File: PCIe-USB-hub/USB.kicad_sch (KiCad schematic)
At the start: 8 parts, among them J2 USB3_A_Stacked, J3 USB3_A_Stacked, J4 USB3_A_Stacked, J5 USB3_A_Stacked, J6 USB3_A_Stacked, J7 USB3_A_Stacked, J8 USB3_A_Stacked, J9 USB3_A_Stacked

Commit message: Частично добавил компоненты
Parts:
- removed J7, J8, J9: USB3_A_Stacked, Connector_USB:USB3_A_Molex_48406-0001_Horizontal_Stacked, symbol Connector:USB3_A_Stacked
- added C1, C10, C2, C3, C4, C5, C6, C7, C8, C9: EEEFK1E151P, Capacitor_SMD:C_Elec_8x10.2, symbol Device:C_Polarized
- added DD3: TPS2552DRVR, Package_SON:WSON-6-1EP_2x2mm_P0.65mm_EP1x1.6mm, symbol TPS2552DRVR:TPS2552DRVR
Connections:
- net at J4.10 (VBUS2): now also C3.1
- net at J3.10 (VBUS2): now also C9.1
- net at J6.10 (VBUS2): now also C6.1
- net at J5.1 (VBUS1): now also C7.1
- net at J5.10 (VBUS2): now also C10.1
- net at J6.1 (VBUS1): now also C5.1
- net at J2.10 (VBUS2): now also C2.1
- net at J3.1 (VBUS1): now also C8.1
- net at J4.1 (VBUS1): now also C4.1
- net at J2.1 (VBUS1): now also C1.1
- new net Earth: C1.2, C10.2, C2.2, C3.2, C4.2, C5.2, C6.2, C7.2, C8.2, C9.2
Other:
- moved on the sheet: J2A, J2B, J3A, J3B, J4A, J4B, J5A, J5B, J6A, J6B

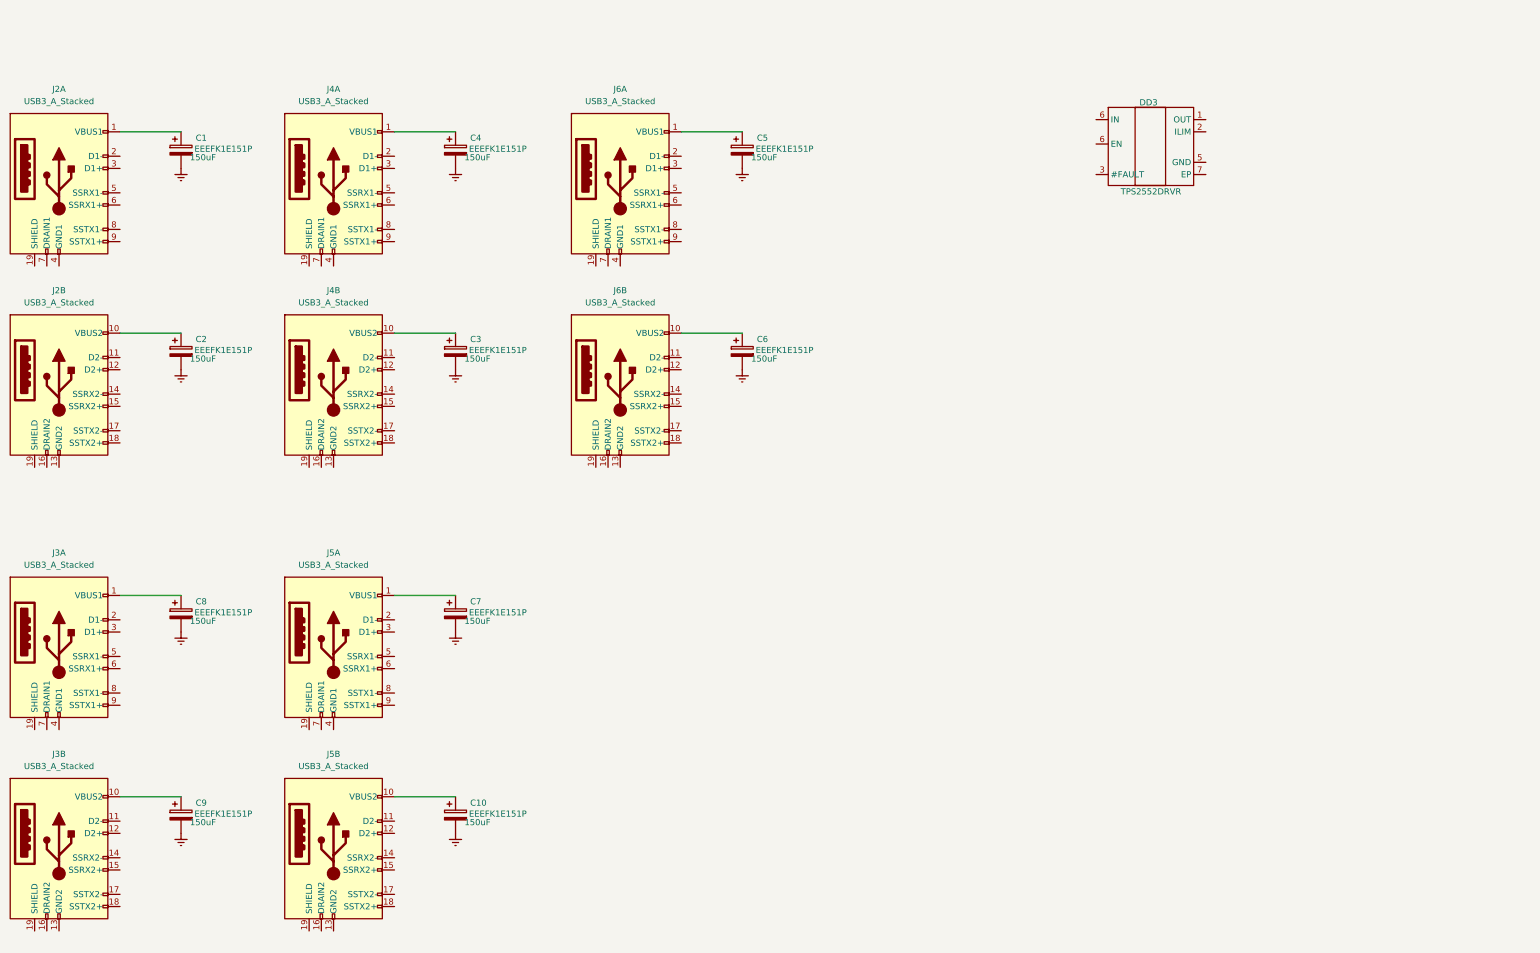
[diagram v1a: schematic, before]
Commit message: Изменение иерархии схемы + на схеме теперь все линии USB соединены
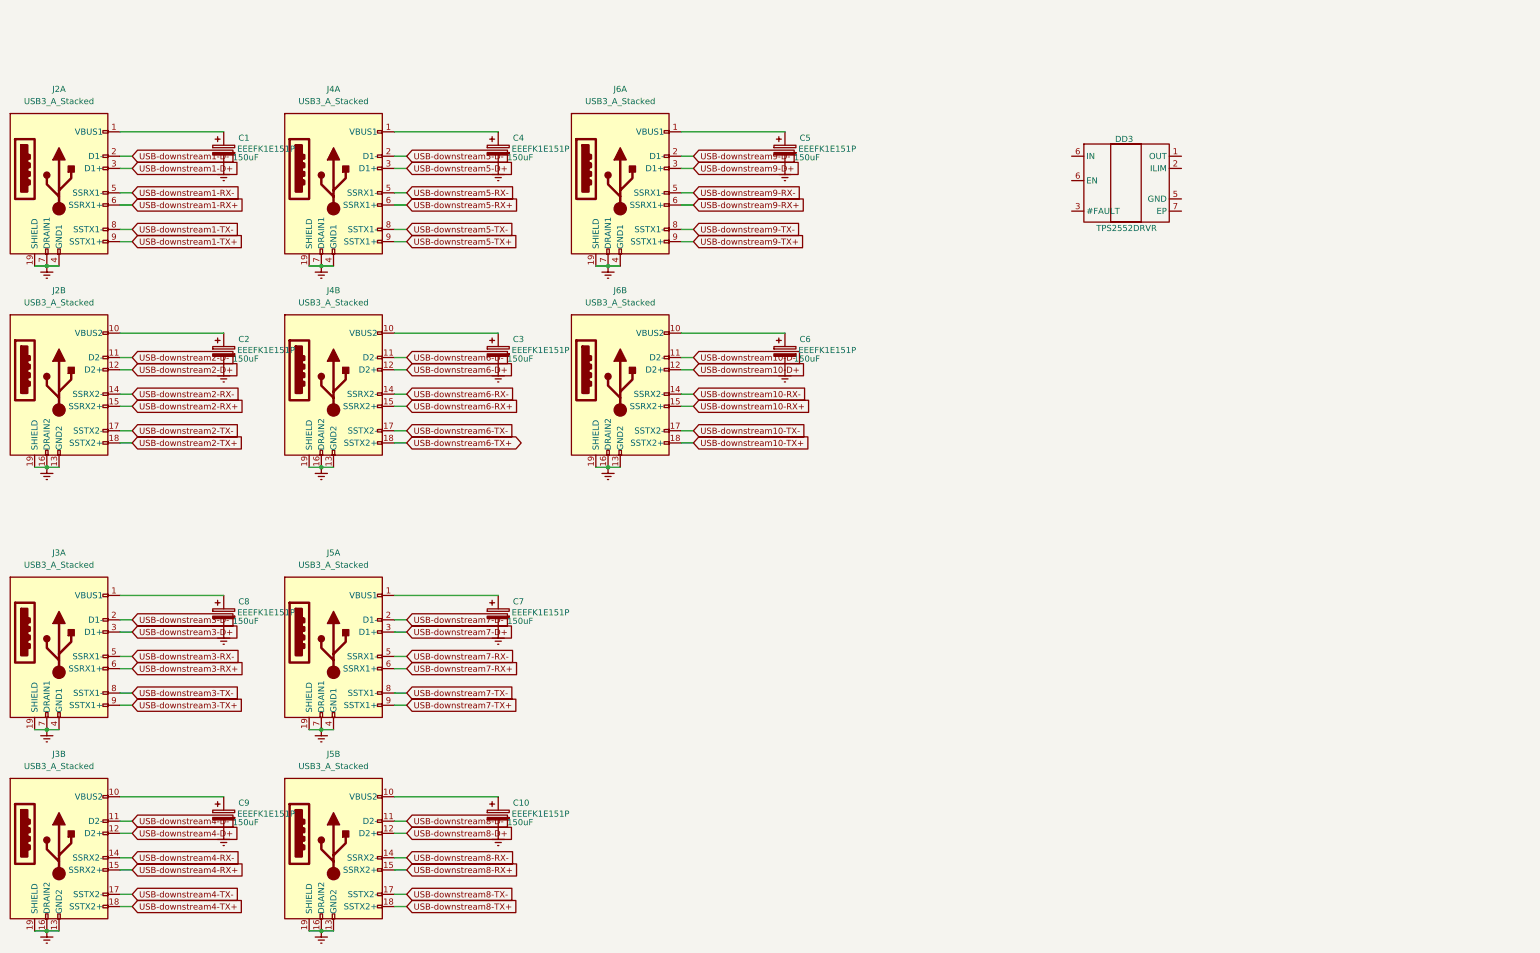
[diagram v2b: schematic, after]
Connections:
- net Earth: now also J2.13 (GND2), J2.16 (DRAIN2), J2.19 (SHIELD), J2.19 (SHIELD), J2.4 (GND1), J2.7 (DRAIN1), J3.13 (GND2), J3.16 (DRAIN2), J3.19 (SHIELD), J3.19 (SHIELD), J3.4 (GND1), J3.7 (DRAIN1), J4.13 (GND2), J4.16 (DRAIN2), J4.19 (SHIELD), J4.19 (SHIELD), J4.4 (GND1), J4.7 (DRAIN1), J5.13 (GND2), J5.16 (DRAIN2), J5.19 (SHIELD), J5.19 (SHIELD), J5.4 (GND1), J5.7 (DRAIN1), J6.13 (GND2), J6.16 (DRAIN2), J6.19 (SHIELD), J6.19 (SHIELD), J6.4 (GND1), J6.7 (DRAIN1)
- net USB-downstream6-D-: now reaches J4.11 (D2-)
- net USB-downstream6-D+: now reaches J4.12 (D2+)
- net USB-downstream6-RX-: now reaches J4.14 (SSRX2-)
- net USB-downstream6-RX+: now reaches J4.15 (SSRX2+)
- net USB-downstream6-TX-: now reaches J4.17 (SSTX2-)
- net USB-downstream6-TX+: now reaches J4.18 (SSTX2+)
- net USB-downstream4-D-: now reaches J3.11 (D2-)
- net USB-downstream4-D+: now reaches J3.12 (D2+)
- net USB-downstream4-RX-: now reaches J3.14 (SSRX2-)
- net USB-downstream4-RX+: now reaches J3.15 (SSRX2+)
- net USB-downstream4-TX-: now reaches J3.17 (SSTX2-)
- net USB-downstream4-TX+: now reaches J3.18 (SSTX2+)
- net USB-downstream10-D-: now reaches J6.11 (D2-)
- net USB-downstream10-D+: now reaches J6.12 (D2+)
- net USB-downstream10-RX-: now reaches J6.14 (SSRX2-)
- net USB-downstream10-RX+: now reaches J6.15 (SSRX2+)
- net USB-downstream10-TX-: now reaches J6.17 (SSTX2-)
- net USB-downstream10-TX+: now reaches J6.18 (SSTX2+)
- net USB-downstream7-D-: now reaches J5.2 (D1-)
- net USB-downstream7-D+: now reaches J5.3 (D1+)
- net USB-downstream7-RX-: now reaches J5.5 (SSRX1-)
- net USB-downstream7-RX+: now reaches J5.6 (SSRX1+)
- net USB-downstream7-TX-: now reaches J5.8 (SSTX1-)
- net USB-downstream7-TX+: now reaches J5.9 (SSTX1+)
- net USB-downstream8-D-: now reaches J5.11 (D2-)
- net USB-downstream8-D+: now reaches J5.12 (D2+)
- net USB-downstream8-RX-: now reaches J5.14 (SSRX2-)
- net USB-downstream8-RX+: now reaches J5.15 (SSRX2+)
- net USB-downstream8-TX-: now reaches J5.17 (SSTX2-)
- net USB-downstream8-TX+: now reaches J5.18 (SSTX2+)
- net USB-downstream9-D-: now reaches J6.2 (D1-)
- net USB-downstream9-D+: now reaches J6.3 (D1+)
- net USB-downstream9-RX-: now reaches J6.5 (SSRX1-)
- net USB-downstream9-RX+: now reaches J6.6 (SSRX1+)
- net USB-downstream9-TX-: now reaches J6.8 (SSTX1-)
- net USB-downstream9-TX+: now reaches J6.9 (SSTX1+)
- net USB-downstream2-D-: now reaches J2.11 (D2-)
- net USB-downstream2-D+: now reaches J2.12 (D2+)
- net USB-downstream2-RX-: now reaches J2.14 (SSRX2-)
- net USB-downstream2-RX+: now reaches J2.15 (SSRX2+)
- net USB-downstream2-TX-: now reaches J2.17 (SSTX2-)
- net USB-downstream2-TX+: now reaches J2.18 (SSTX2+)
- net USB-downstream3-D-: now reaches J3.2 (D1-)
- net USB-downstream3-D+: now reaches J3.3 (D1+)
- net USB-downstream3-RX-: now reaches J3.5 (SSRX1-)
- net USB-downstream3-RX+: now reaches J3.6 (SSRX1+)
- net USB-downstream3-TX-: now reaches J3.8 (SSTX1-)
- net USB-downstream3-TX+: now reaches J3.9 (SSTX1+)
- net USB-downstream5-D-: now reaches J4.2 (D1-)
- net USB-downstream5-D+: now reaches J4.3 (D1+)
- net USB-downstream5-RX-: now reaches J4.5 (SSRX1-)
- net USB-downstream5-RX+: now reaches J4.6 (SSRX1+)
- net USB-downstream5-TX-: now reaches J4.8 (SSTX1-)
- net USB-downstream5-TX+: now reaches J4.9 (SSTX1+)
- net USB-downstream1-D-: now reaches J2.2 (D1-)
- net USB-downstream1-D+: now reaches J2.3 (D1+)
- net USB-downstream1-RX-: now reaches J2.5 (SSRX1-)
- net USB-downstream1-RX+: now reaches J2.6 (SSRX1+)
- net USB-downstream1-TX-: now reaches J2.8 (SSTX1-)
- net USB-downstream1-TX+: now reaches J2.9 (SSTX1+)
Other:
- moved on the sheet: C1, C10, C2, C3, C4, C5, C6, C7, C8, C9, DD3

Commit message: Исправил отсутствие перекрёстного соединения на  PCIe
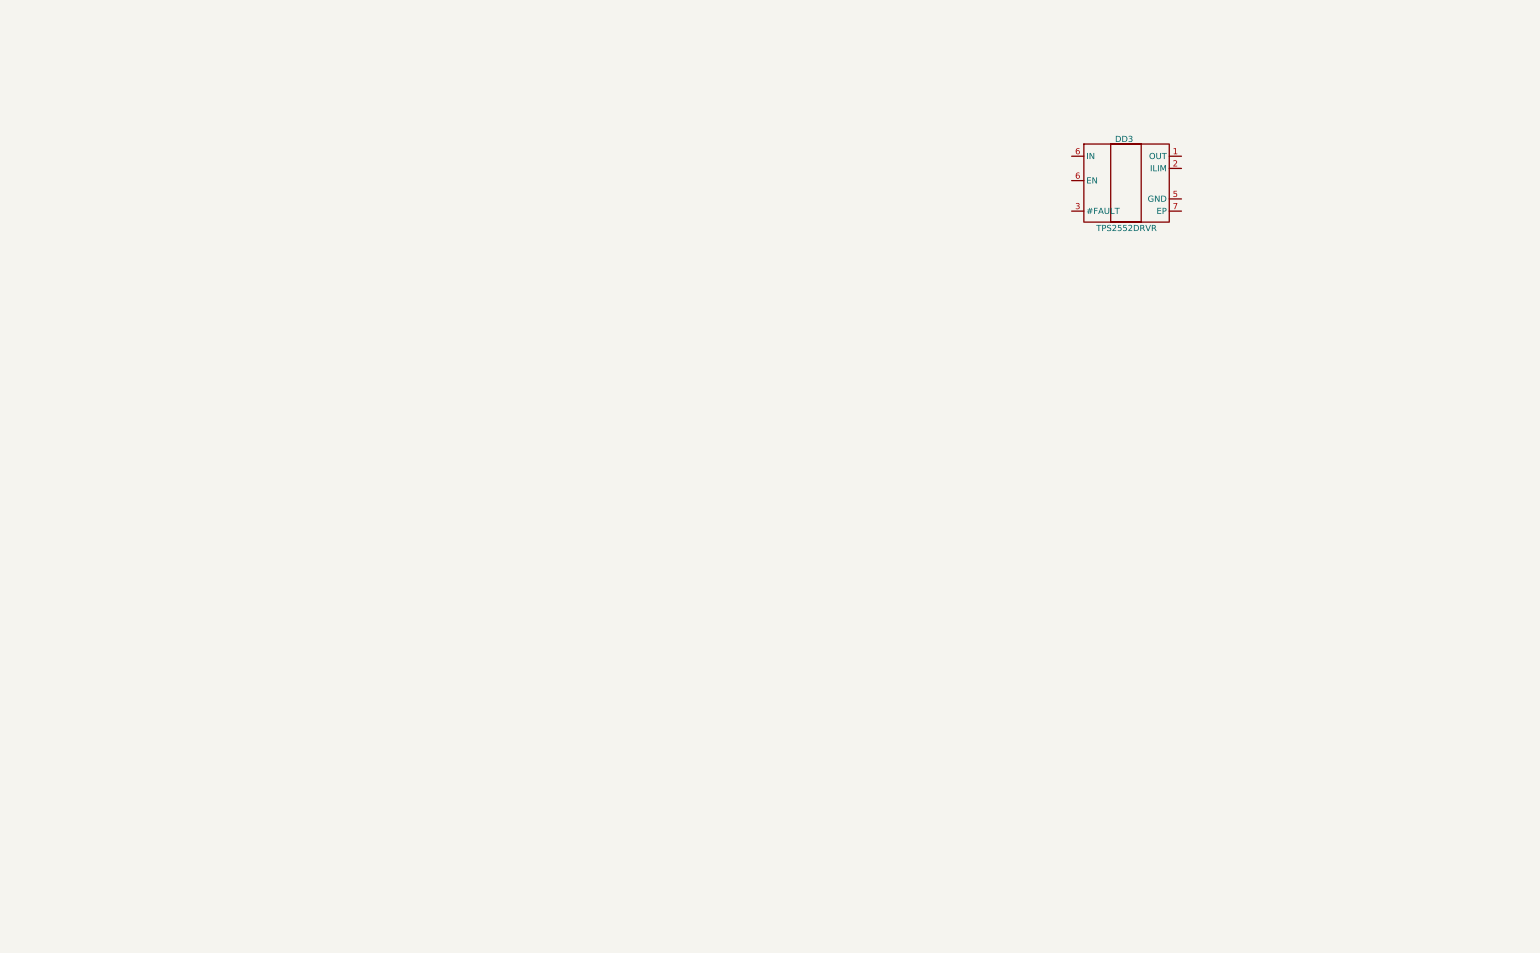
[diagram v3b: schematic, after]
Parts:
- removed C1, C10, C2, C3, C4, C5, C6, C7, C8, C9: EEEFK1E151P, Capacitor_SMD:C_Elec_8x10.2, symbol Device:C_Polarized
- removed J2, J3, J4, J5, J6: USB3_A_Stacked, Connector_USB:USB3_A_Molex_48406-0001_Horizontal_Stacked, symbol Connector:USB3_A_Stacked
